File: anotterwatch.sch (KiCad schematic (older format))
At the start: 0 parts

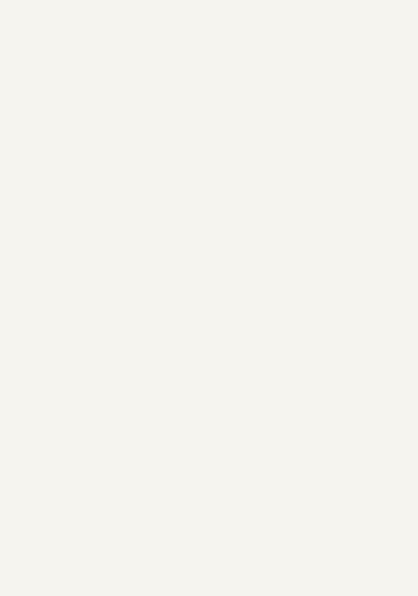
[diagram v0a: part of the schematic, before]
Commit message: added USB-C connector
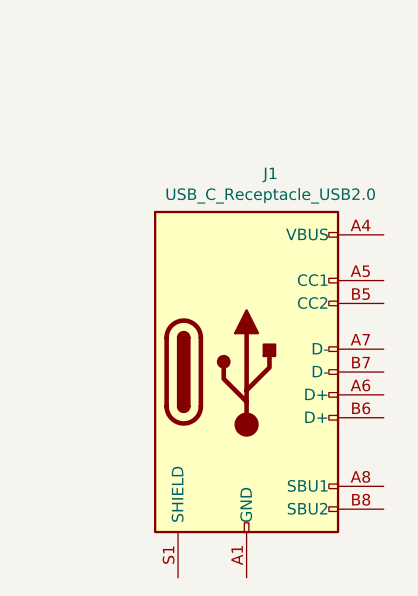
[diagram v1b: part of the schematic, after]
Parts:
- added J1: USB_C_Receptacle_USB2.0, badgelib:USB-C 16Pin, symbol Connector:USB_C_Receptacle_USB2.0
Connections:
- new net GND: J1.A1 (GND), J1.A12 (GND), J1.B1 (GND), J1.B12 (GND)
- new net VBUS: J1.A4 (VBUS), J1.A9 (VBUS), J1.B4 (VBUS), J1.B9 (VBUS)
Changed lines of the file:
@@
 Text Notes 500  1150 0    50   ~ 0
 Todo: \nESP \nSerial-USB (with esd) \nUSB-C (lib has to be drawn) \nDisplay AFE (niklas) \nRGB LED \nWhite LED \nSensors (TBD)
+$Comp
+L Connector:USB_C_Receptacle_USB2.0 J1
+U 1 1 5C6DC086
+P 1500 2950
+F 0 "J1" H 1605 3817 50  0000 C CNN
+F 1 "USB_C_Receptacle_USB2.0" H 1605 3726 50  0000 C CNN
+F 2 "badgelib:USB-C 16Pin" H 1650 2950 50  0001 C CNN
+F 3 "https://www.usb.org/sites/default/files/documents/usb_type-c.zip" H 1650 2950 50  0001 C CNN
+	1    1500 2950
+	1    0    0    -1
+$EndComp
 $EndSCHEMATC

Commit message: added sk6812
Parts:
- added C1: 100p, symbol Device:C_Small
- added C2, C3: 100n, symbol Device:C_Small
- added D1, D2: SK6812, badgelib:sk6812_side, symbol LED:SK6812
- added R1, R2: 5k1, symbol Device:R_Small
- added U1: USBLC6-4SC6, Package_TO_SOT_SMD:SOT-23-6, symbol Power_Protection:USBLC6-2SC6
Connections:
- net labels added: Dn, Dp, GND, VBUS, VDD, sk6812
- wire segments 0 -> 31
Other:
- note added: "Todo: \nESP \nSerial-USB (with esd) \nDisplay AFE (niklas) \nRGB LED \nWhite LED \nSensors (TBD)\nButtons"
- note removed: "Todo: \nESP \nSerial-USB (with esd) \nUSB-C (lib has to be drawn) \nDisplay AFE (niklas) \nRGB LED \nWhite LED \nSensors (TBD)"

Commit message: added led
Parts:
- added D3: LED, badgelib:RZX-S020CCW-0.4T, symbol Device:LED
- added Q1: Q_NMOS_GSD, Package_TO_SOT_SMD:SOT-23, symbol Device:Q_NMOS_GSD
- added R3: 100, symbol Device:R_Small
- added R4: 10k, symbol Device:R_Small
- added R5: R_LED (150mA), symbol Device:R_Small
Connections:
- net labels added: +BATT, LED
- wire segments 31 -> 40
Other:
- note added: "Todo: \nESP \nSerial-USB (with esd) \nDisplay\nAFE (niklas) \nSensors (TBD)\nButtons\nBattery\n"
- note removed: "Todo: \nESP \nSerial-USB (with esd) \nDisplay AFE (niklas) \nRGB LED \nWhite LED \nSensors (TBD)\nButtons"
- moved on the sheet: C2, C3, D1, D2

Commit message: added datasheets
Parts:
- removed D1: SK6812, badgelib:sk6812_side, symbol LED:SK6812
- added D?: SK6812, badgelib:sk6812_side, symbol LED:SK6812
- D2: Type (none) -> SK6812 4020
- D3: Type (none) -> RZX-S020CCW-0.4T
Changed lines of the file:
@@
 	2000 5200 2150 5200
-$Comp
-L LED:SK6812 D1
-U 1 1 5C6E3DDA
-P 1250 6950
-F 0 "D1" H 1591 6996 50  0000 L CNN
-F 1 "SK6812" H 1591 6905 50  0000 L CNN
-F 2 "badgelib:sk6812_side" H 1300 6650 50  0001 L TNN
-F 3 "https://cdn-shop.adafruit.com/product-files/1138/SK6812+LED+datasheet+.pdf" H 1350 6575 50  0001 L TNN
-	1    1250 6950
-	1    0    0    -1
-$EndComp
 $Comp
 L LED:SK6812 D2
@@
 F 1 "SK6812" H 2591 6905 50  0000 L CNN
 F 2 "badgelib:sk6812_side" H 2300 6650 50  0001 L TNN
-F 3 "https://cdn-shop.adafruit.com/product-files/1138/SK6812+LED+datasheet+.pdf" H 2350 6575 50  0001 L TNN
+F 3 "https://de.aliexpress.com/item/10-3000-st-cke-SK6812-4020-Seite-Emmitting-RGB-LED-mit-eingebauten-SK6812-IC-SMD-4020/32877531241.html" H 2350 6575 50  0001 L TNN
+F 4 "SK6812 4020" H 2250 6950 50  0001 C CNN "Type"
 	1    2250 6950
 	1    0    0    -1
@@
 F 1 "LED" V 4847 6583 50  0000 R CNN
 F 2 "badgelib:RZX-S020CCW-0.4T" H 4900 6700 50  0001 C CNN
-F 3 "~" H 4900 6700 50  0001 C CNN
+F 3 "https://de.aliexpress.com/item/2000-st-cke-Rolle-Ultra-slim-0-4mm-seite-view-LED-020-SMD-geeignet-f-r/32920375451.html" H 4900 6700 50  0001 C CNN
+F 4 "RZX-S020CCW-0.4T" V 4900 6700 50  0001 C CNN "Type"
 	1    4900 6700
 	0    -1   -1   0
@@
 Wire Wire Line
 	4050 7100 4200 7100
+$Comp
+L LED:SK6812 D?
+U 1 1 5C6F42D3
+P 1250 6950
+F 0 "D?" H 1591 6996 50  0000 L CNN
+F 1 "SK6812" H 1591 6905 50  0000 L CNN
+F 2 "badgelib:sk6812_side" H 1300 6650 50  0001 L TNN
+F 3 "https://de.aliexpress.com/item/10-3000-st-cke-SK6812-4020-Seite-Emmitting-RGB-LED-mit-eingebauten-SK6812-IC-SMD-4020/32877531241.html" H 1350 6575 50  0001 L TNN
+F 4 "SK6812 4020" H 1250 6950 50  0001 C CNN "Type"
+	1    1250 6950
+	1    0    0    -1
+$EndComp
 $EndSCHEMATC

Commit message: fixed lib
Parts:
- added U?: ST7789V, symbol badgelib:ST7789V
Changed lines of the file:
@@
 EESchema Schematic File Version 4
+LIBS:anotterwatch-cache
 EELAYER 26 0
 EELAYER END
@@
 	1    0    0    -1
 $EndComp
+$Comp
+L badgelib:ST7789V U?
+U 1 1 5C7D4E59
+P 5700 3900
+F 0 "U?" H 5650 4550 50  0000 L CNN
+F 1 "ST7789V" H 5550 4450 50  0000 L CNN
+F 2 "" H 6600 4350 50  0001 C CNN
+F 3 "https://cdn-shop.adafruit.com/product-files/3787/FRD154B12001-A.pdf" H 6600 4350 50  0001 C CNN
+	1    5700 3900
+	1    0    0    -1
+$EndComp

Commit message: added display + datasheet, removed VDD added VCC
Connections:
- net labels added: VCC
- net labels removed: VDD
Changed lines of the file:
@@
-	1    0    0    -1
-$EndComp
-$Comp
-L power:VBUS #PWR0105
-U 1 1 5C6E25E7
-P 1500 4700
-F 0 "#PWR0105" H 1500 4550 50  0001 C CNN
-F 1 "VBUS" H 1515 4873 50  0000 C CNN
-F 2 "" H 1500 4700 50  0001 C CNN
-F 3 "" H 1500 4700 50  0001 C CNN
-	1    1500 4700
 	1    0    0    -1
 $EndComp
@@
 Wire Wire Line
 	1950 6950 1550 6950
-$Comp
-L power:VDD #PWR0107
-U 1 1 5C6E428D
-P 2250 6600
-F 0 "#PWR0107" H 2250 6450 50  0001 C CNN
-F 1 "VDD" H 2267 6773 50  0000 C CNN
-F 2 "" H 2250 6600 50  0001 C CNN
-F 3 "" H 2250 6600 50  0001 C CNN
-	1    2250 6600
-	1    0    0    -1
-$EndComp
-$Comp
-L power:VDD #PWR0108
-U 1 1 5C6E42D2
-P 1250 6600
-F 0 "#PWR0108" H 1250 6450 50  0001 C CNN
-F 1 "VDD" H 1267 6773 50  0000 C CNN
-F 2 "" H 1250 6600 50  0001 C CNN
-F 3 "" H 1250 6600 50  0001 C CNN
-	1    1250 6600
-	1    0    0    -1
-$EndComp
 Wire Wire Line
 	1250 6600 1250 6650
@@
 	1    0    0    -1
 $EndComp
-$Comp
-L power:VDD #PWR0111
-U 1 1 5C6E55B6
-P 3050 6800
-F 0 "#PWR0111" H 3050 6650 50  0001 C CNN
-F 1 "VDD" H 3067 6973 50  0000 C CNN
-F 2 "" H 3050 6800 50  0001 C CNN
-F 3 "" H 3050 6800 50  0001 C CNN
-	1    3050 6800
-	1    0    0    -1
-$EndComp
 Wire Wire Line
 	3050 6800 3050 6850
@@
 F 3 "~" H 3400 6950 50  0001 C CNN
 	1    3400 6950
-	1    0    0    -1
-$EndComp
-$Comp
-L power:VDD #PWR0113
-U 1 1 5C6E6349
-P 3400 6800
-F 0 "#PWR0113" H 3400 6650 50  0001 C CNN
-F 1 "VDD" H 3417 6973 50  0000 C CNN
-F 2 "" H 3400 6800 50  0001 C CNN
-F 3 "" H 3400 6800 50  0001 C CNN
-	1    3400 6800
 	1    0    0    -1
 $EndComp
@@
 	1    0    0    -1
 $EndComp
+$Comp
+L power:VCC #PWR?
+U 1 1 5C7D5C54
+P 3400 6800
+F 0 "#PWR?" H 3400 6650 50  0001 C CNN
+F 1 "VCC" H 3417 6973 50  0000 C CNN
+F 2 "" H 3400 6800 50  0001 C CNN
+F 3 "" H 3400 6800 50  0001 C CNN
+	1    3400 6800
+	1    0    0    -1
+$EndComp
+$Comp
+L power:VCC #PWR?
+U 1 1 5C7D6EA0
+P 3050 6800
+F 0 "#PWR?" H 3050 6650 50  0001 C CNN
+F 1 "VCC" H 3067 6973 50  0000 C CNN
+F 2 "" H 3050 6800 50  0001 C CNN
+F 3 "" H 3050 6800 50  0001 C CNN
+	1    3050 6800
+	1    0    0    -1
+$EndComp
+$Comp
+L power:VCC #PWR?
+U 1 1 5C7D6EEF
+P 2250 6600
+F 0 "#PWR?" H 2250 6450 50  0001 C CNN
+F 1 "VCC" H 2267 6773 50  0000 C CNN
+F 2 "" H 2250 6600 50  0001 C CNN
+F 3 "" H 2250 6600 50  0001 C CNN
+	1    2250 6600
+	1    0    0    -1
+$EndComp
+$Comp
+L power:VCC #PWR?
+U 1 1 5C7D6F3E
+P 1250 6600
+F 0 "#PWR?" H 1250 6450 50  0001 C CNN
+F 1 "VCC" H 1267 6773 50  0000 C CNN
+F 2 "" H 1250 6600 50  0001 C CNN
+F 3 "" H 1250 6600 50  0001 C CNN
+	1    1250 6600
+	1    0    0    -1
+$EndComp
+$Comp
+L power:VCC #PWR?
+U 1 1 5C7D70BA
+P 1500 4700
+F 0 "#PWR?" H 1500 4550 50  0001 C CNN
+F 1 "VCC" H 1517 4873 50  0000 C CNN
+F 2 "" H 1500 4700 50  0001 C CNN
+F 3 "" H 1500 4700 50  0001 C CNN
+	1    1500 4700
+	1    0    0    -1
+$EndComp

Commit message: added reset circuit
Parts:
- added C? (x4): 100n, symbol Device:C_Small
- added Q?: nfet, Package_TO_SOT_SMD:SOT-23, symbol Device:Q_NMOS_GSD
- added Q? (x2): npn, symbol Device:Q_NPN_BEC
- added R? (x3): 10k, symbol Device:R_Small
- added U?: CH340G, Package_SO:SOIC-16_3.9x9.9mm_P1.27mm, symbol Interface_USB:CH340G
- U?: symbol badgelib:ST7789V -> anotterwatch-rescue:ST7789V-badgelib
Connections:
- net labels added: CH340_V3, DTR, EN, IO0, IPS_CD, IPS_CS, IPS_LED, IPS_MOSI, IPS_SCK, RTS, RXD, TXD, White_LED
- net labels removed: LED
- wire segments 40 -> 59
- no-connect marks 0 -> 7

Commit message: added esp
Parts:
- added U?: ESP32, ESP32-footprints-Lib:ESP32, symbol ESP32-footprints-Shem-Lib:ESP32
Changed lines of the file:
@@
 Text GLabel 10950 3800 1    50   Input ~ 0
 EN
+$Comp
+L ESP32-footprints-Shem-Lib:ESP32 U?
+U 1 1 5C71E383
+P 5050 3500
+F 0 "U?" H 5050 5337 60  0000 C CNN
+F 1 "ESP32" H 5050 5231 60  0000 C CNN
+F 2 "ESP32-footprints-Lib:ESP32" H 5050 1875 60  0001 C CNN
+F 3 "https://www.espressif.com/sites/default/files/documentation/esp32-pico-d4_datasheet_en.pdf" H 5500 4400 60  0001 C CNN
+F 4 "https://github.com/adamjvr/ESP32-kiCAD-Footprints" H 5050 3500 50  0001 C CNN "Lib"
+	1    5050 3500
+	1    0    0    -1
+$EndComp
 $EndSCHEMATC
